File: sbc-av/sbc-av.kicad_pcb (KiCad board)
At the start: 4 copper layers, 17.8 x 38.1 mm, 42 parts, among them J1 AVD-Header, J2 AVA-Header, Q1 PZT2222A, U1 MAX1683, U2 CD74HCT367E, U3 FMS6400

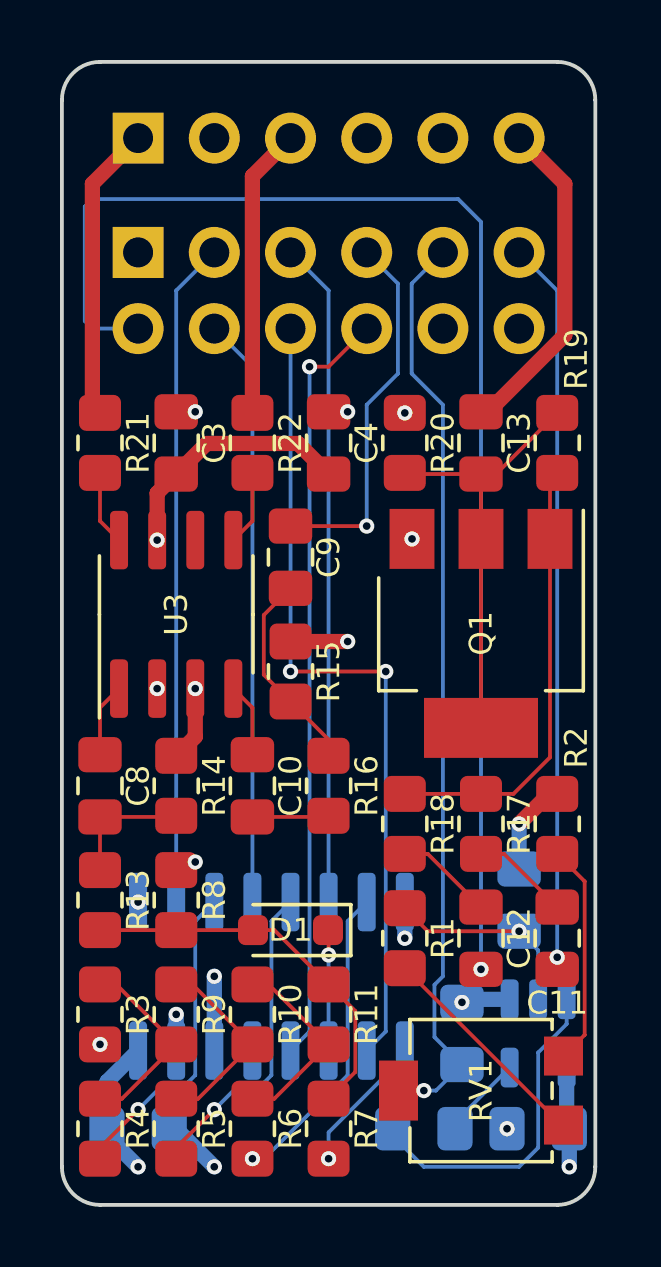
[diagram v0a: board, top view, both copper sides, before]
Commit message: SBC v1.3
Motherboard updates:

  - KiCad 9 upgrade
  - USB-C power connector
  - Replace EOL resistor packs with discrete SMD resistors
  - Power/enable voltage translators from switched 5V
  - Fix motor signal pullup
  - Eliminate loop in phi2 traces
  - Thicker clock signal traces

SD card adapter updates:

  - KiCad 9 upgrade
  - Power/enable voltage translator from switched 5V and the eliminate unnecessary SIO pullups

Audio/Video adapter updates:

  - KiCad 9 upgrade
  - No functional changes, gerbers not regenerated, cleaned up bom
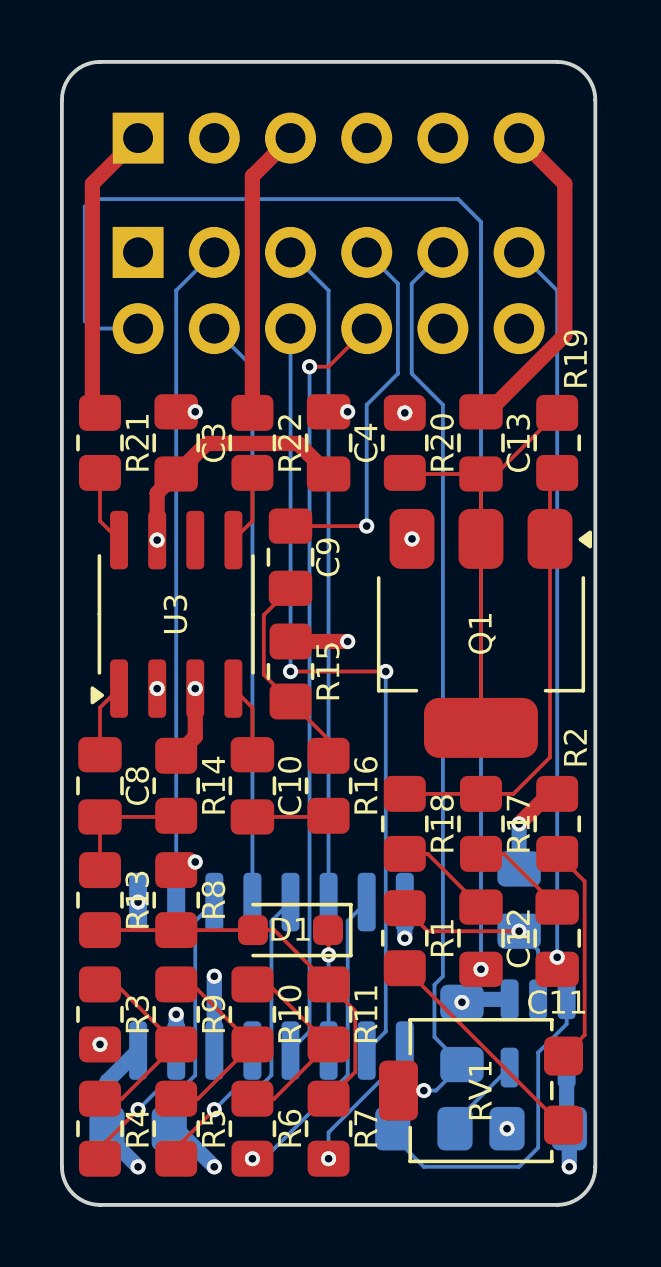
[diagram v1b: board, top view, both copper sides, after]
